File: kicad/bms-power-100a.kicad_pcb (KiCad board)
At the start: 4 copper layers, 132 x 65 mm, 48 parts, among them P1 CONN_01X01, P2 CONN_01X01, P3 CONN_01X01, P4 CONN_01X01, Q1 Q_NMOS_GDS, Q10 Q_NMOS_GDS, Q11 Q_NMOS_GDS, Q12 Q_NMOS_GDS, Q13 Q_NMOS_GDS, Q14 Q_NMOS_GDS, Q15 Q_NMOS_GDS, Q16 Q_NMOS_GDS, Q17 Q_NMOS_GDS, Q18 Q_NMOS_GDS, Q19 Q_NMOS_GDS, Q2 Q_NMOS_GDS, Q20 Q_NMOS_GDS, Q21 ZXMP6A13F, Q3 Q_NMOS_GDS, Q4 Q_NMOS_GDS, Q5 Q_NMOS_GDS, Q6 Q_NMOS_GDS, Q7 Q_NMOS_GDS, Q8 Q_NMOS_GDS, Q9 Q_NMOS_GDS

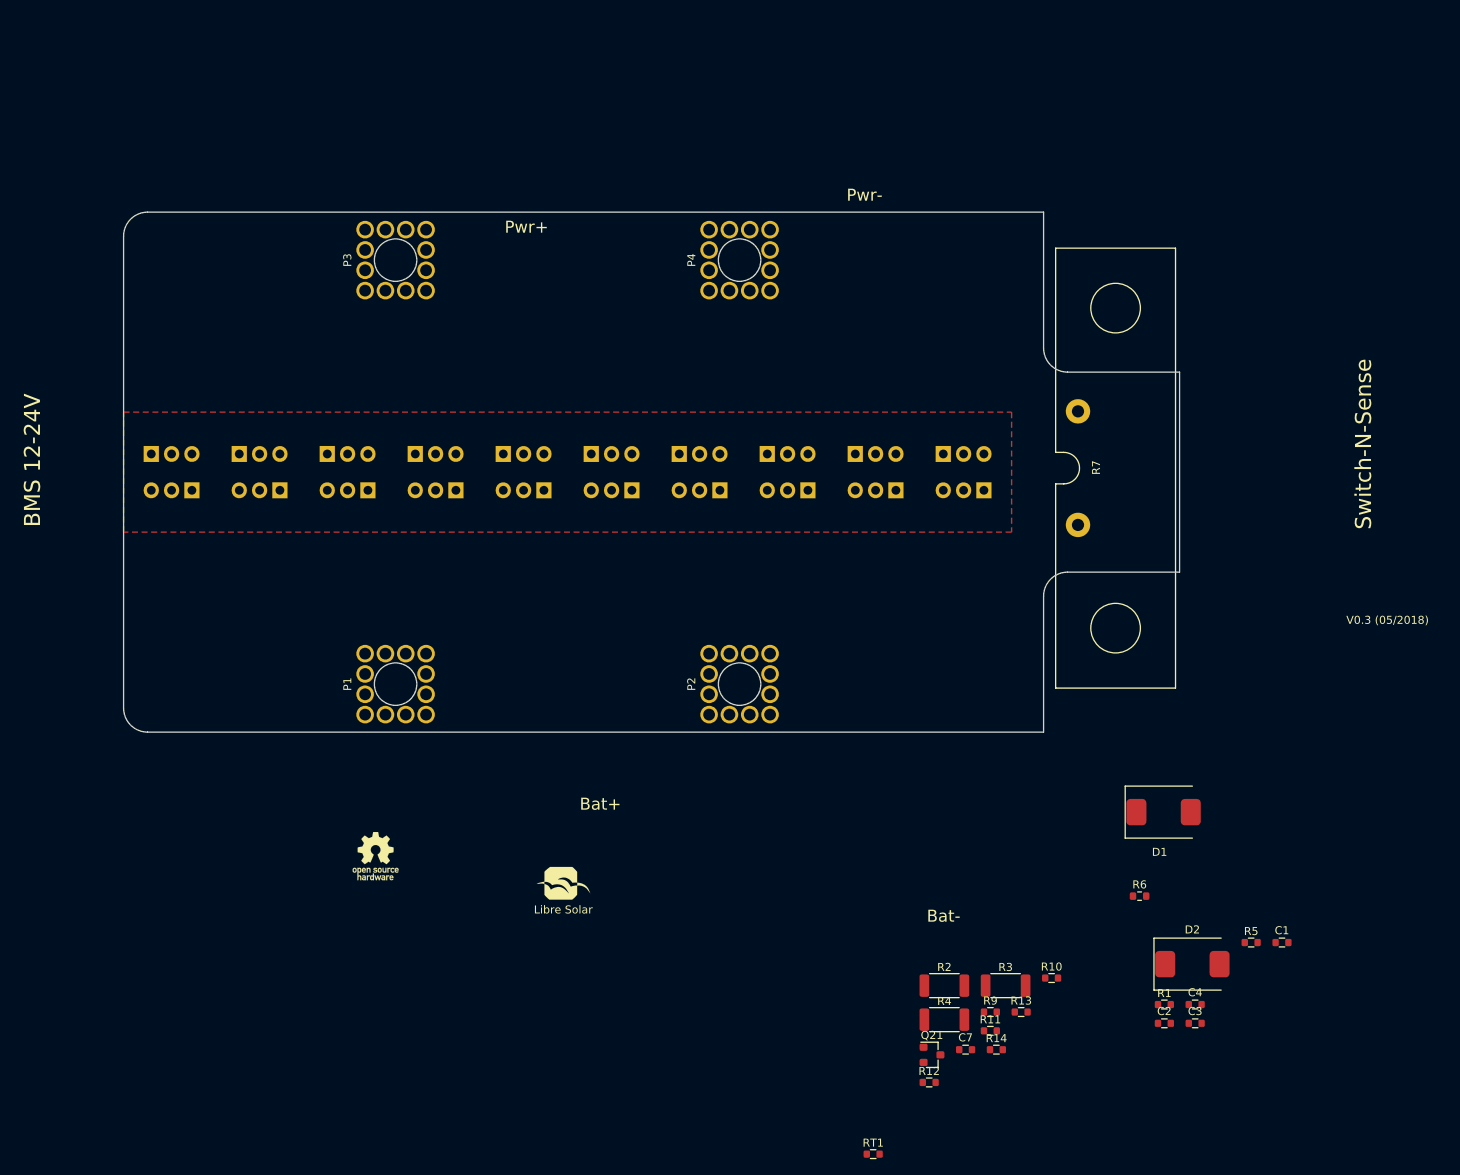
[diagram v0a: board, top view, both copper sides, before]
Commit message: Update KiCad files based on spec updates
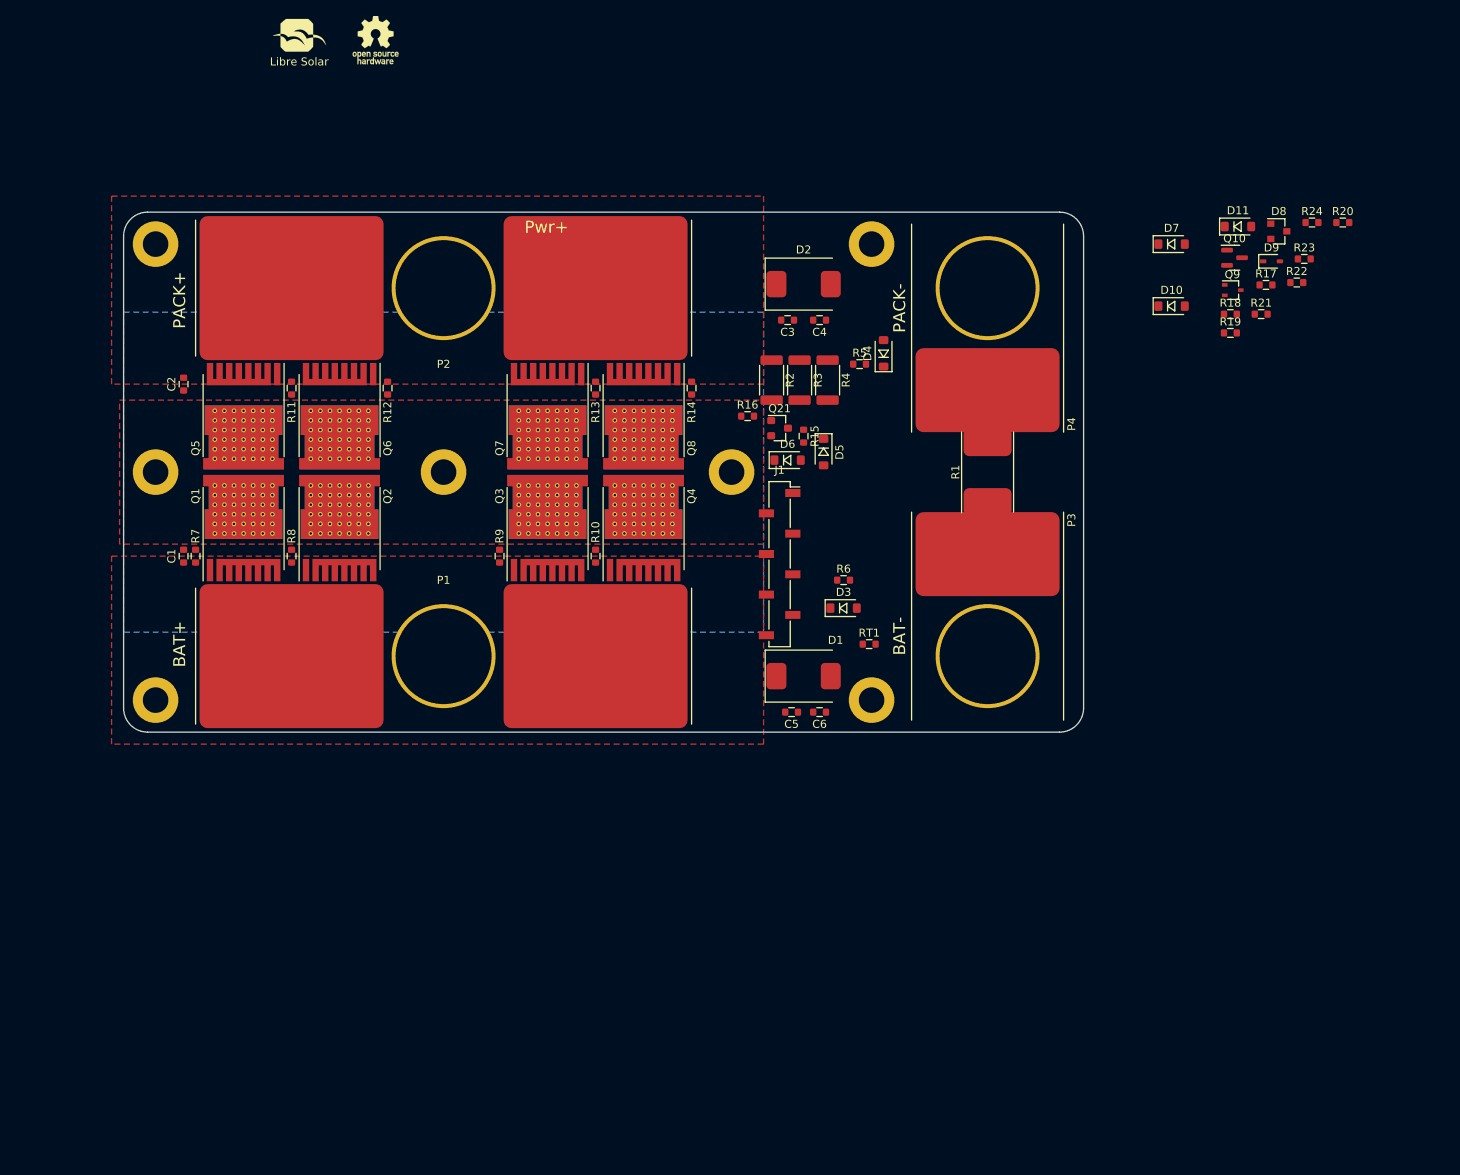
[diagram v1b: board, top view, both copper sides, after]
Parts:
- removed C7: 10n, LibreSolar:C_0603_1608
- removed Q15, Q16, Q17, Q18, Q19, Q20: Q_NMOS_GDS, LibreSolar:TO-220-3_Horizontal_TabUp_NoHole
- removed the Q5 at (132.5, 89.8)
- removed the Q6 at (143.5, 89.8)
- removed the Q7 at (154.5, 89.8)
- removed the Q8 at (165.5, 89.8)
- removed the R6 at (207.0, 140.5)
- added C5: 100n, LibreSolar:C_0603_1608, F.Cu at (163.5, 117.5)
- added C6: 100n, LibreSolar:C_0603_1608, F.Cu at (167.0, 117.5)
- added D10: BAT46W-7-F, LibreSolar:D_SOD-123, F.Cu at (211.0, 66.8)
- added D11: 16V, LibreSolar:D_SOD-123, F.Cu at (219.3, 56.8)
- added D3: 16V, LibreSolar:D_SOD-123, F.Cu at (170.0, 104.5)
- added D4: 16V, LibreSolar:D_SOD-123, F.Cu at (175.0, 72.7)
- added D5: 75V, LibreSolar:D_SOD-123, F.Cu at (167.5, 85.0)
- added D6: 16V, LibreSolar:D_SOD-123, F.Cu at (163.0, 86.0)
- added D7: BAT46W-7-F, LibreSolar:D_SOD-123, F.Cu at (211.0, 59.0)
- added D8: BAS16,215, Diode_SMD:D_SOT-23_ANK, F.Cu at (224.4, 57.4)
- added D9: 5.1V, LibreSolar:D_SOD-323, F.Cu at (223.5, 61.1)
- added H1: MountingHole, MountingHole:MountingHole_3.2mm_M3_ISO7380_Pad, F.Cu at (84.0, 87.5)
- added H2: MountingHole, MountingHole:MountingHole_3.2mm_M3_ISO7380_Pad, F.Cu at (120.0, 87.5)
- added H3: MountingHole, MountingHole:MountingHole_3.2mm_M3_ISO7380_Pad, F.Cu at (156.0, 87.5)
- added H4: MountingHole, MountingHole:MountingHole_3.2mm_M3_ISO7380_Pad, F.Cu at (84.0, 116.0)
- added H5: MountingHole, MountingHole:MountingHole_3.2mm_M3_ISO7380_Pad, F.Cu at (173.5, 59.0)
- added H6: MountingHole, MountingHole:MountingHole_3.2mm_M3_ISO7380_Pad, F.Cu at (84.0, 59.0)
- added H7: MountingHole, MountingHole:MountingHole_3.2mm_M3_ISO7380_Pad, F.Cu at (173.5, 116.0)
- added J1: Conn_01x08, Connector_PinSocket_2.54mm:PinSocket_1x08_P2.54mm_Vertical_SMD_Pin1Right, F.Cu at (162.0, 99.0)
- added R1: 500µ, LibreSolar:R_Shunt_3920, F.Cu at (188.0, 87.5)
- added R15: 68k, LibreSolar:R_0603_1608, F.Cu at (165.0, 83.0)
- added R16: 1M, LibreSolar:R_0603_1608, F.Cu at (158.0, 80.5)
- added R17: 100, LibreSolar:R_0603_1608, F.Cu at (222.8, 64.1)
- added R18: 100, LibreSolar:R_0603_1608, F.Cu at (218.3, 67.8)
- added R19: 1k, LibreSolar:R_0603_1608, F.Cu at (218.3, 70.1)
- added R20: 56k, LibreSolar:R_0603_1608, F.Cu at (232.4, 56.3)
- added R21: 100, LibreSolar:R_0603_1608, F.Cu at (222.2, 67.8)
- added R22: 100, LibreSolar:R_0603_1608, F.Cu at (226.7, 63.8)
- added R23: 10M, LibreSolar:R_0603_1608, F.Cu at (227.6, 60.9)
- added R24: 10k, LibreSolar:R_0603_1608, F.Cu at (228.6, 56.3)
- added R8: 51, LibreSolar:R_0603_1608, F.Cu at (101.0, 98.0)
- D1, D2: value SMCJ24A -> SMCJ60A
- P1, P2: footprint LibreSolar:Wuerth_WP-BUCF_7460408 -> LibreSolar:Busbar_100A_Wide
- P3, P4: footprint LibreSolar:Wuerth_WP-BUCF_7460408 -> LibreSolar:Busbar_100A_Short
- Q1, Q2, Q3, Q4: value Q_NMOS_GDS -> IPT015N10N5; footprint LibreSolar:TO-220-3_Horizontal_TabUp_NoHole -> Package_TO_SOT_SMD:Infineon_PG-HSOF-8-1_ThermalVias; moved to F.Cu
- Q10: value Q_NMOS_GDS -> BSS123N; footprint LibreSolar:TO-220-3_Horizontal_TabUp_NoHole -> Package_TO_SOT_SMD:SOT-23; moved to F.Cu
- Q5: renamed from Q11; value Q_NMOS_GDS -> IPT015N10N5; footprint LibreSolar:TO-220-3_Horizontal_TabUp_NoHole -> Package_TO_SOT_SMD:Infineon_PG-HSOF-8-1_ThermalVias; moved to F.Cu
- Q6: renamed from Q12; value Q_NMOS_GDS -> IPT015N10N5; footprint LibreSolar:TO-220-3_Horizontal_TabUp_NoHole -> Package_TO_SOT_SMD:Infineon_PG-HSOF-8-1_ThermalVias; moved to F.Cu
- Q7: renamed from Q13; value Q_NMOS_GDS -> IPT015N10N5; footprint LibreSolar:TO-220-3_Horizontal_TabUp_NoHole -> Package_TO_SOT_SMD:Infineon_PG-HSOF-8-1_ThermalVias; moved to F.Cu
- Q8: renamed from Q14; value Q_NMOS_GDS -> IPT015N10N5; footprint LibreSolar:TO-220-3_Horizontal_TabUp_NoHole -> Package_TO_SOT_SMD:Infineon_PG-HSOF-8-1_ThermalVias; moved to F.Cu
- Q9: value Q_NMOS_GDS -> DMG1013UW; footprint LibreSolar:TO-220-3_Horizontal_TabUp_NoHole -> Package_TO_SOT_SMD:SOT-323_SC-70; moved to F.Cu
- R10, R11, R9: value 1k -> 51
- R12, R13: value 4.7 -> 51
- R14: value 100 -> 51
- R5: value 1M -> 10M
- R6: renamed from R1; value 1M -> 10M
- R7: value 2m -> 51; footprint LibreSolar:R_Shunt_Vishay_WSMS5515 -> LibreSolar:R_0603_1608
- moved C2 146.3 mm to (87.5, 76.5), turned to 90 degrees
- moved C1 145.5 mm to (87.5, 98.0), turned to 90 degrees
- moved R7 123.6 mm to (89.0, 98.0), turned to -90 degrees
- moved R11 118.7 mm to (101.0, 77.0), turned to -90 degrees
- moved LOGO2 111.0 mm to (99.7, 34.9)
- moved R12 110.1 mm to (113.0, 77.0), turned to -90 degrees
- moved LOGO1 102.0 mm to (111.5, 33.5)
- moved C3 101.6 mm to (163.0, 68.5)
- moved D2 97.9 mm to (165.0, 64.0)
- moved C4 97.6 mm to (167.0, 68.5)
- moved R13 94.4 mm to (139.0, 77.0), turned to -90 degrees
- moved R14 91.0 mm to (151.0, 77.0), turned to -90 degrees
- moved P3 89.0 mm to (188.0, 110.5)
- moved R5 87.3 mm to (172.0, 74.0)
- moved R9 83.7 mm to (127.0, 98.0), turned to -90 degrees
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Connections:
- C2 pad 2: /LOAD+ -> /PACK+
- C3 pad 1: /LOAD+ -> /PACK+
- C4 pad 2: unconnected-(C4-Pad2) -> /PACK-
- D1 pad 1: unconnected-(D1-Pad1) -> /BAT+
- D1 pad 2: unconnected-(D1-Pad2) -> GND
- D2 pad 1: unconnected-(D2-Pad1) -> /PACK+
- D2 pad 2: unconnected-(D2-Pad2) -> /PACK-
- P2 pad 1: /BAT+ -> /PACK+
- P3 pad 1: /LOAD+ -> GND
- P4 pad 1: /LOAD+ -> /PACK-
- Q1 pad 1: /CHG_G -> Net-(R7-Pad2)
- Q1 pad 2: /CHG+ -> /BAT+
- Q1 pad 3: /BAT+ -> /CD
- Q10 pad 1: unconnected-(Q10-Pad1) -> Net-(D10-Pad1)
- Q10 pad 2: unconnected-(Q10-Pad2) -> /PACK+
- Q10 pad 3: unconnected-(Q10-Pad3) -> Net-(Q10-Pad3)
- Q2 pad 1: /CHG_G -> Net-(Q2-Pad1)
- Q2 pad 2: /CHG+ -> /BAT+
- Q2 pad 3: /BAT+ -> /CD
- Q21 pad 1: /PCHG_G -> Net-(D6-Pad2)
- Q21 pad 2: Net-(Q21-Pad2) -> /CD
- Q21 pad 3: /LOAD+ -> Net-(Q21-Pad3)
- Q3 pad 1: unconnected-(Q3-Pad1) -> Net-(Q3-Pad1)
- Q3 pad 2: unconnected-(Q3-Pad2) -> /BAT+
- Q3 pad 3: unconnected-(Q3-Pad3) -> /CD
- Q4 pad 1: unconnected-(Q4-Pad1) -> Net-(Q4-Pad1)
- Q4 pad 2: unconnected-(Q4-Pad2) -> /BAT+
- Q4 pad 3: unconnected-(Q4-Pad3) -> /CD
- Q5 pad 1: /DSG_G -> Net-(R11-Pad1)
- Q5 pad 2: /CHG+ -> /PACK+
- Q5 pad 3: /LOAD+ -> /CD
- Q6 pad 1: /DSG_G -> Net-(Q6-Pad1)
- Q6 pad 2: /CHG+ -> /PACK+
- Q6 pad 3: /LOAD+ -> /CD
- Q7 pad 1: unconnected-(Q13-Pad1) -> Net-(Q7-Pad1)
- Q7 pad 2: unconnected-(Q13-Pad2) -> /PACK+
- Q7 pad 3: unconnected-(Q13-Pad3) -> /CD
- Q8 pad 1: unconnected-(Q14-Pad1) -> Net-(Q8-Pad1)
- Q8 pad 2: unconnected-(Q14-Pad2) -> /PACK+
- Q8 pad 3: unconnected-(Q14-Pad3) -> /CD
- Q9 pad 1: unconnected-(Q9-Pad1) -> Net-(D8-Pad1)
- Q9 pad 2: unconnected-(Q9-Pad2) -> Net-(R12-Pad2)
- Q9 pad 3: unconnected-(Q9-Pad3) -> Net-(Q9-Pad3)
- R10 pad 1: unconnected-(R10-Pad1) -> Net-(R10-Pad1)
- R10 pad 2: /DSG_EN -> Net-(Q4-Pad1)
- R11 pad 1: unconnected-(R11-Pad1) -> Net-(R11-Pad1)
- R11 pad 2: /PCHG_EN -> Net-(R12-Pad2)
- R12 pad 1: /CHG_G -> Net-(Q6-Pad1)
- R12 pad 2: unconnected-(R12-Pad2) -> Net-(R12-Pad2)
- R13 pad 1: /DSG_G -> Net-(Q7-Pad1)
- R13 pad 2: unconnected-(R13-Pad2) -> Net-(R12-Pad2)
- R14 pad 1: Net-(C7-Pad1) -> Net-(Q8-Pad1)
- R14 pad 2: /LOAD+ -> Net-(R12-Pad2)
- R2 pad 1: Net-(Q21-Pad2) -> /PACK+
- R2 pad 2: /CHG+ -> Net-(Q21-Pad3)
- R3 pad 1: Net-(Q21-Pad2) -> /PACK+
- R3 pad 2: /CHG+ -> Net-(Q21-Pad3)
- R4 pad 1: Net-(Q21-Pad2) -> /PACK+
- R4 pad 2: /CHG+ -> Net-(Q21-Pad3)
- R5 pad 1: /LOAD+ -> Net-(R12-Pad2)
- R5 pad 2: /DSG_G -> /PACK+
- R6 pad 1: /CHG_G -> Net-(R10-Pad1)
- R7 pad 1: GND -> Net-(R10-Pad1)
- R7 pad 2: /LOAD- -> Net-(R7-Pad2)
- R9 pad 1: unconnected-(R9-Pad1) -> Net-(R10-Pad1)
- R9 pad 2: /CHG_EN -> Net-(Q3-Pad1)
- RT1 pad 1: unconnected-(RT1-Pad1) -> Net-(RT1-Pad1)
- RT1 pad 2: unconnected-(RT1-Pad2) -> Net-(RT1-Pad2)
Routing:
- added copper zone on F.Cu, net /BAT+
- added copper zone on B.Cu, net /CD
- added copper zone on F.Cu, net /CD
- added copper zone on F.Cu, net /PACK+
- removed copper zone on F.Cu, net /CHG+
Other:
- board size 132 x 65 mm -> 120 x 65 mm
- board text added: "BAT+"
- board text added: "BAT-"
- board text added: "PACK+"
- board text added: "PACK-"
- board text removed: "BMS 12-24V"
- board text removed: "Bat+"
- board text removed: "Bat-"
- board text removed: "Pwr-"
- board text removed: "Switch-N-Sense"
- board text removed: "V0.3 (05/2018)"

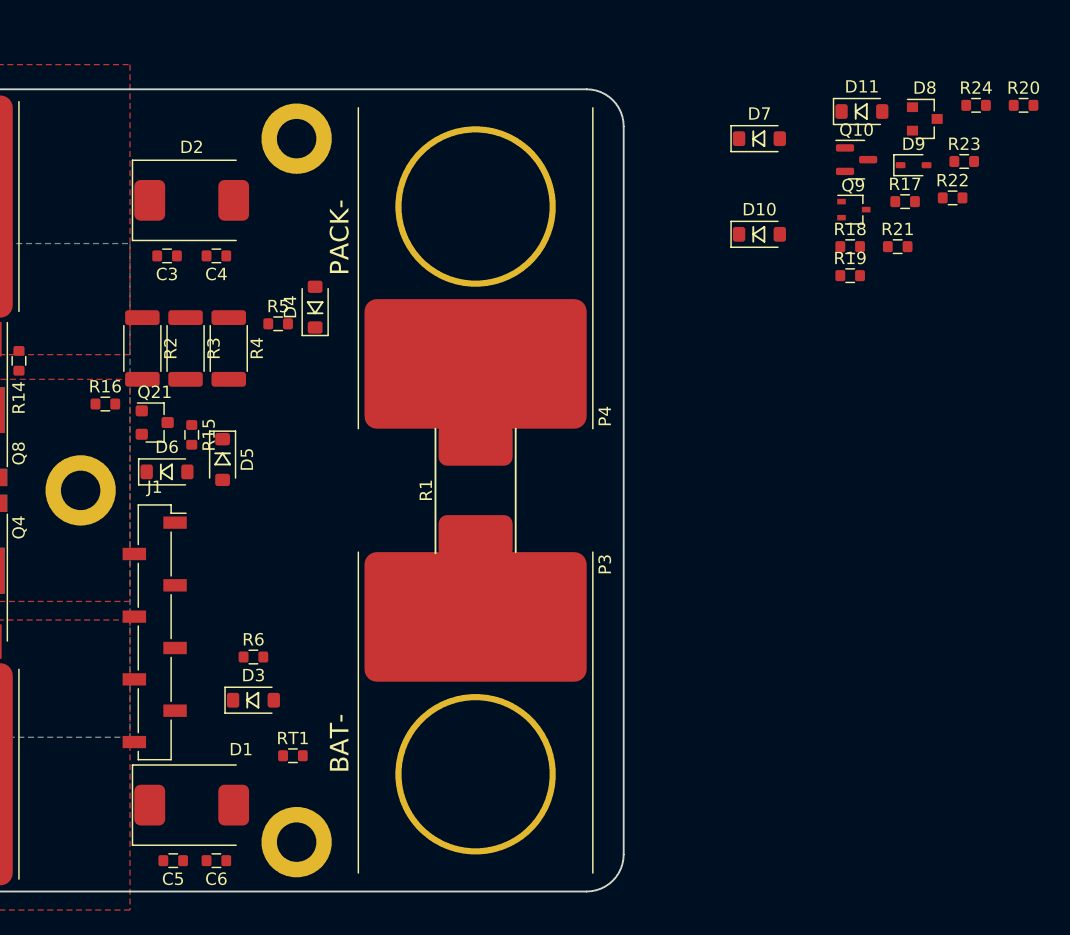
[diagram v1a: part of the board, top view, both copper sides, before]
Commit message: WIP: Schematic almost finished
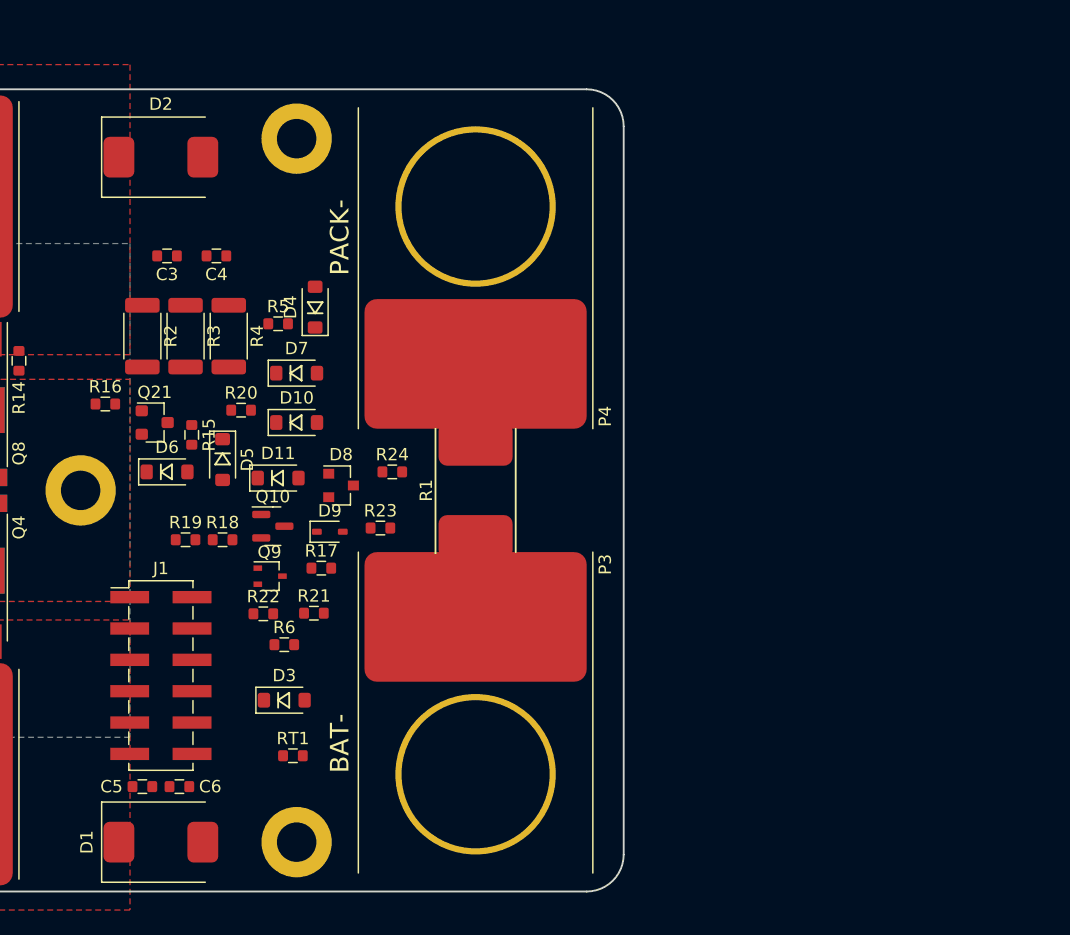
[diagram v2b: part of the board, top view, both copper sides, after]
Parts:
- J1: value Conn_01x08 -> Conn_02x06_Odd_Even; footprint Connector_PinSocket_2.54mm:PinSocket_1x08_P2.54mm_Vertical_SMD_Pin1Right -> Connector_PinHeader_2.54mm:PinHeader_2x06_P2.54mm_Vertical_SMD
- moved R20 68.0 mm to (169.0, 81.0)
- moved R22 65.2 mm to (170.8, 97.5)
- moved R19 57.9 mm to (164.5, 91.5)
- moved R18 56.1 mm to (167.5, 91.5)
- moved D11 55.9 mm to (172.0, 86.5)
- moved D8 55.9 mm to (177.1, 87.1)
- moved D9 55.9 mm to (176.2, 90.8)
- moved Q10 55.9 mm to (171.6, 90.4)
- moved Q9 55.9 mm to (171.3, 94.5)
- moved R17 55.9 mm to (175.5, 93.8)
- moved R23 55.9 mm to (180.3, 90.5)
- moved R24 55.9 mm to (181.2, 86.0)
- moved R21 55.9 mm to (174.9, 97.5)
- moved D7 42.0 mm to (173.5, 78.0)
- moved D10 40.5 mm to (173.5, 82.0)
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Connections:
- J1 pad 4: /PACK+ -> unconnected-(J1-Pad4)
- J1 pad 5: /PACK- -> /PACK+
- J1 pad 6: /BAT- -> unconnected-(J1-Pad6)
- J1 pad 7: Net-(RT1-Pad1) -> /CHG+
- J1 pad 8: Net-(RT1-Pad2) -> /PACK-
- Q1 pad 3: /CD -> /CHG+
- Q2 pad 3: /CD -> /CHG+
- Q3 pad 3: /CD -> /CHG+
- Q4 pad 3: /CD -> /CHG+
- Q5 pad 3: /CD -> /CHG+
- Q6 pad 3: /CD -> /CHG+
- Q7 pad 3: /CD -> /CHG+
- Q8 pad 3: /CD -> /CHG+
- RT1 pad 1: Net-(RT1-Pad1) -> Net-(J1-Pad12)
- RT1 pad 2: Net-(RT1-Pad2) -> Net-(J1-Pad11)
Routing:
- added copper zone on B.Cu, net /CHG+
- removed copper zone on B.Cu, net /CD

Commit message: v0.1 design ready for review
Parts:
- removed H7: MountingHole, MountingHole:MountingHole_3.2mm_M3_ISO7380_Pad
- removed R3, R4: 330, LibreSolar:R_2010_5025
- added FID1: Fiducial, Fiducial:Fiducial_1mm_Mask2mm, F.Cu at (85.0, 97.5)
- added FID2: Fiducial, Fiducial:Fiducial_1mm_Mask2mm, F.Cu at (177.0, 67.5)
- added J2: Conn_01x06, Connector_PinHeader_2.00mm:PinHeader_1x06_P2.00mm_Vertical_SMD_Pin1Left, F.Cu at (161.0, 111.0)
- added REF**: WEEE-Logo_4.2x6mm_SilkScreen, Symbol:WEEE-Logo_4.2x6mm_SilkScreen, F.Cu at (119.0, 95.5)
- J1: value Conn_02x06_Odd_Even -> Conn_01x06; footprint Connector_PinHeader_2.54mm:PinHeader_2x06_P2.54mm_Vertical_SMD -> Connector_PinHeader_2.00mm:PinHeader_1x06_P2.00mm_Vertical_SMD_Pin1Left
- P1, P2: footprint LibreSolar:Busbar_100A_Wide -> LibreSolar:Busbar_100A_Long_Stud
- P3, P4: footprint LibreSolar:Busbar_100A_Short -> LibreSolar:Busbar_100A_Short_Stud
- R2: value 330 -> 40; footprint LibreSolar:R_2010_5025 -> Package_TO_SOT_SMD:TO-252-2
- moved H4 115.1 mm to (195.5, 87.5)
- moved H6 109.9 mm to (178.0, 116.0)
- moved LOGO2 95.5 mm to (166.7, 102.9)
- moved LOGO1 45.6 mm to (119.0, 78.5)
- moved J1 38.5 mm to (161.0, 64.0), turned to 90 degrees
- moved P1 31.0 mm to (89.0, 111.0)
- moved P2 31.0 mm to (89.0, 64.0)
- moved RT1 27.5 mm to (149.5, 95.0), turned to -90 degrees
- moved R18 22.8 mm to (164.0, 69.0)
- moved R17 21.3 mm to (158.0, 106.0), turned to 90 degrees
- moved R19 18.0 mm to (165.8, 73.5), turned to -90 degrees
- moved D6 17.8 mm to (159.8, 68.5)
- moved D8 16.5 mm to (171.8, 71.5), turned to 90 degrees
- moved R21 16.2 mm to (170.8, 81.8), turned to 90 degrees
- moved Q9 16.0 mm to (171.5, 78.5), turned to -90 degrees
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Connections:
- net Net-(D3-Pad1) renamed /CHG_G
- net Net-(D4-Pad1) renamed /DSG_G
- D6 pad 1: /CD -> /CHG+
- J1 pad 1: /CHG -> /PACK+
- J1 pad 2: /DSG -> unconnected-(J1-Pad2)
- J1 pad 4: unconnected-(J1-Pad4) -> /DSG
- J1 pad 5: /PACK+ -> GND
- J1 pad 6: unconnected-(J1-Pad6) -> /PACK-
- Q21 pad 2: /CD -> /CHG+
- R16 pad 1: /CD -> /CHG+
- R2 pad 1: /PACK+ -> Net-(Q21-Pad3)
- R2 pad 2: Net-(Q21-Pad3) -> /CHG+
- RT1 pad 1: Net-(J1-Pad12) -> Net-(J2-Pad5)
- RT1 pad 2: Net-(J1-Pad11) -> Net-(J2-Pad6)
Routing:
- net /CHG_G: track 0.00 -> 77.4 mm
- net /DSG_G: track 0.00 -> 76.6 mm
- net /PACK-: track 0.00 -> 56.8 mm, vias 0 -> 83
- net GND: track 0.00 -> 51.8 mm, vias 0 -> 98
- net /CHG+: track 0.00 -> 39.5 mm, vias 0 -> 162
- net Net-(J2-Pad6): track 0.00 -> 35.0 mm
- net Net-(J2-Pad5): track 0.00 -> 30.4 mm
- net Net-(C1-Pad2): track 0.00 -> 19.1 mm
- net /PACK+: track 0.00 -> 17.8 mm, vias 0 -> 54
- net /PDSG: track 0.00 -> 13.5 mm
- net Net-(D8-Pad1): track 0.00 -> 11.1 mm
- net Net-(D10-Pad1): track 0.00 -> 9.66 mm
- net Net-(D7-Pad1): track 0.00 -> 8.16 mm
- net /DSG: track 0.00 -> 6.67 mm
- net /CHG: track 0.00 -> 6.20 mm
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- added copper zone on B.Cu, net /BAT+
- added copper zone on F.Cu, net /CHG+
- added copper zone on B.Cu, net /PACK+
- added copper zone on B.Cu, net /PACK-
- added copper zone on F.Cu, net /PACK-
- added copper zone on B.Cu, net GND
- added copper zone on F.Cu, net GND
- removed copper zone on F.Cu, net /CD
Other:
- board text added: "2-layer PCB 105 µm copper thickness"
- board text added: "BMS 16S100 SC Power PCB"
- board text added: "v0.1"
- board text removed: "Pwr+"
